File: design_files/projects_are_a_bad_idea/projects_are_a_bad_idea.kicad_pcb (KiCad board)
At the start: 2 copper layers, 26 x 33.1 mm, 3 parts

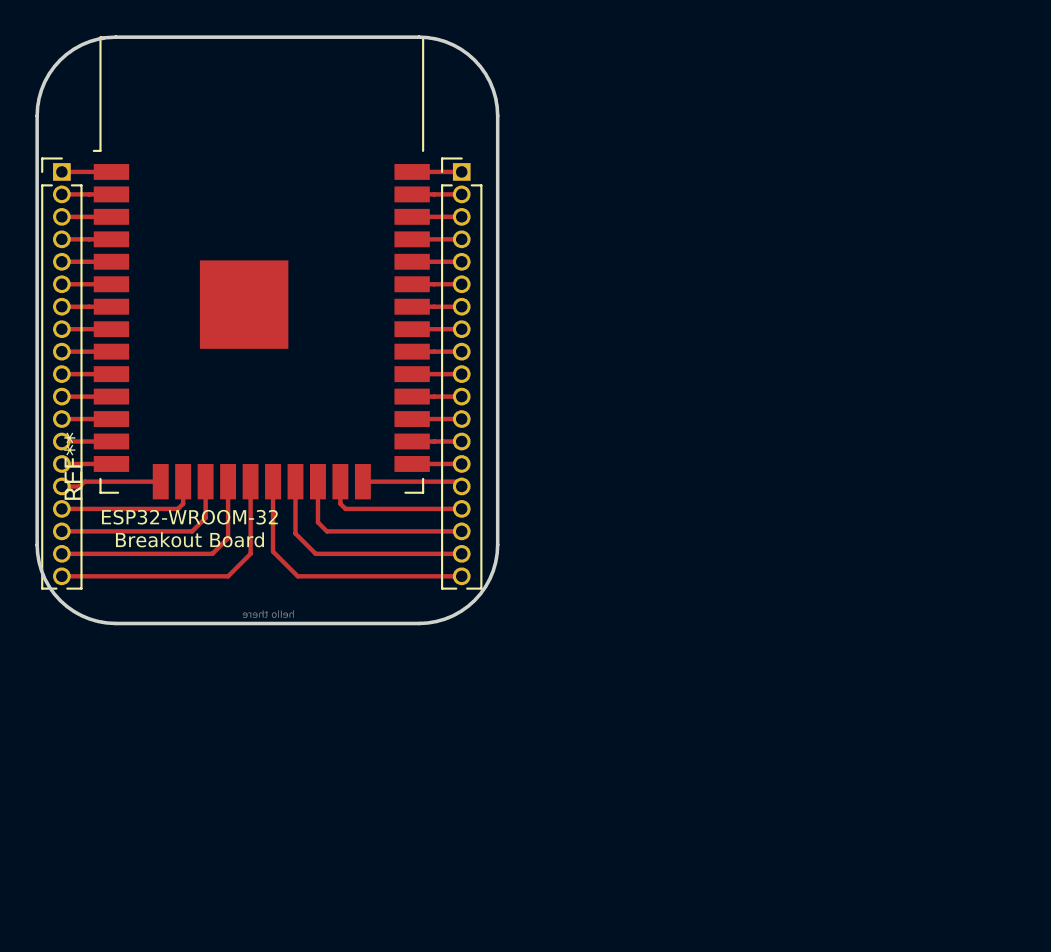
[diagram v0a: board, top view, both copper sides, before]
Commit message: Added basic stopwatch, changed sleep to light sleep
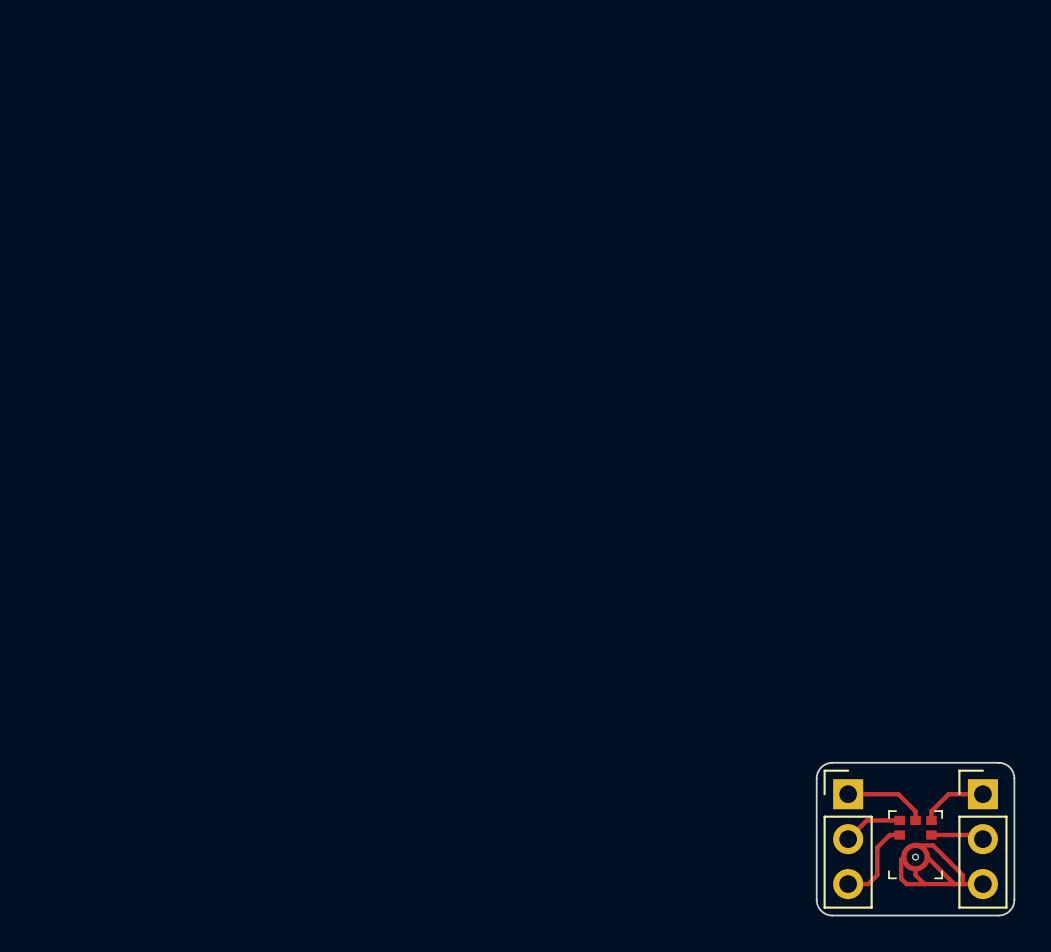
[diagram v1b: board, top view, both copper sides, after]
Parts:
- removed the REF** at (91.4, 53.3)
- removed the REF** at (80.1, 45.1)
- removed the REF** at (102.7, 45.1)
- added ?: , , F.Cu at (128.4, 84.5)
- added REF**: SPH0645LM4H-B-messed-up, DigiKey:SPH0645LM4H-B-messed-up, F.Cu at (128.4, 83.8)
- added REF**: Pin_Header_Straight_1x03_Pitch2.54mm, Pin_Headers:Pin_Header_Straight_1x03_Pitch2.54mm, F.Cu at (124.6, 80.3)
- added REF**: Pin_Header_Straight_1x03_Pitch2.54mm, Pin_Headers:Pin_Header_Straight_1x03_Pitch2.54mm, F.Cu at (132.2, 80.3)
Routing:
- net (no net): track 183.7 -> 33.0 mm
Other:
- board size 26 x 33.1 mm -> 11.2 x 8.6 mm
- rule pad_to_mask_clearance: 0.051 -> 0
- board text added: "BCLK"
- board text added: "Data Out"
- board text added: "GND"
- board text added: "I2S MEMS Microphone"
- board text added: "SELECT"
- board text added: "SPH0645LM4H-B breakout"
- board text added: "VDD"
- board text added: "WS"
- board text removed: "ESP32-WROOM-32 Breakout Board"
- board text removed: "hello there"
